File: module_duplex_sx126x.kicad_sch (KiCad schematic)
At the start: 38 parts, among them J1 USB_B_Mini, J2 Conn_01x06_Pin, J3 Conn_01x05, J4 Conn_01x04, J5 Conn_01x02_Pin, J6 Conn_01x02, SW1 SW_Push, U1 STM32F103C8Tx, U2 AMS1117-3.3, U3 SN65HVD230, U4 Ai-Thinker-Ra-02, U5 Ai-Thinker-Ra-02, Y1 16M, Y2 32.768k

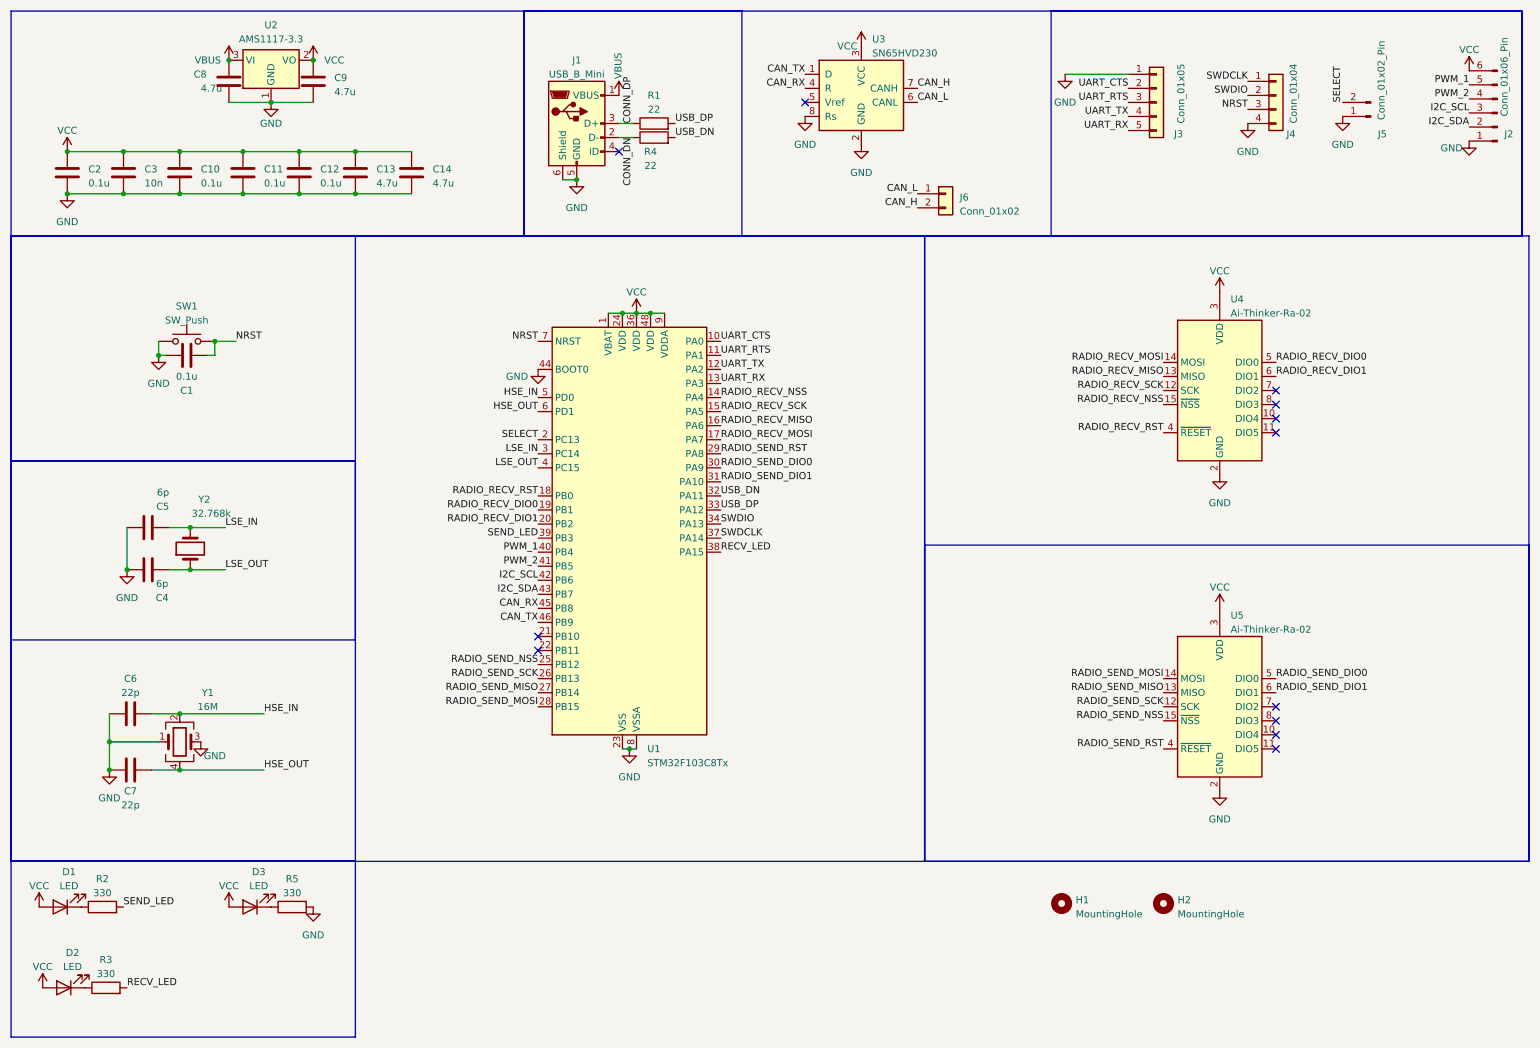
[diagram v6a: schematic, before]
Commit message: Changed connector to jumper; Added USB DM pullup
Signed-off-by: Leonardo Celente <leocelente@gmail.com>
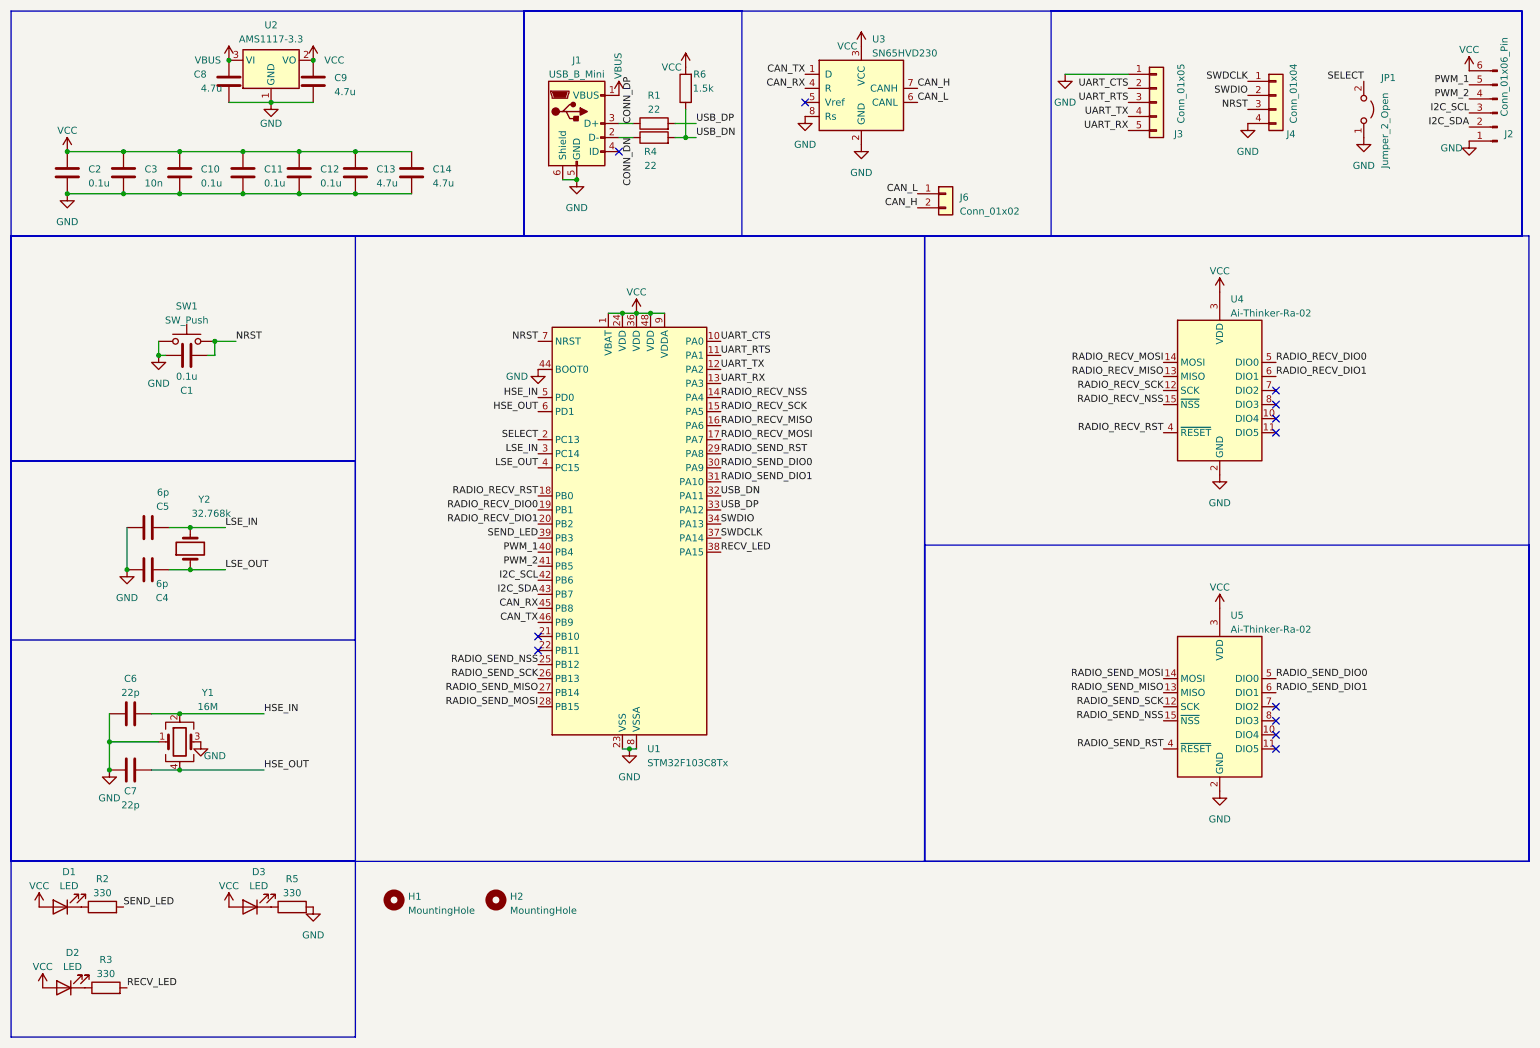
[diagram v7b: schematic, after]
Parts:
- removed J5: Conn_01x02_Pin, Connector_PinHeader_2.54mm:PinHeader_1x02_P2.54mm_Vertical, symbol Connector:Conn_01x02_Pin
- added JP1: Jumper_2_Open, Connector_PinHeader_2.54mm:PinHeader_1x02_P2.54mm_Vertical, symbol Jumper:Jumper_2_Open
- added R6: 1.5k, Resistor_SMD:R_0603_1608Metric, symbol Device:R
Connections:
- net GND: now also JP1.1 (A)
- net SELECT: now also JP1.2 (B)
- net USB_DN: now also R6.1
- net VCC: now also R6.2
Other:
- company: (none) -> Zenith Aerospace (@zenitheesc)
- title: (none) -> SX1262 Duplex USB Module
- moved on the sheet: H1, H2
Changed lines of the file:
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@@
 (kicad_sch (version 20230121) (generator eeschema)
   (paper "A4")
+  (title_block
+    (title "SX1262 Duplex USB Module")
+    (date "2023-05-20")
+    (rev "A")
+    (company "Zenith Aerospace (@zenitheesc)")
+    (comment 1 "Leonardo Celente (@leocelente)")
+  )
   (junction (at 73.66 38.1) (diameter 0) (color 0 0 0 0)
   )
@@
   (junction (at 113.665 43.18) (diameter 0) (color 0 0 0 0)
   )
+  (junction (at 133.35 35.56) (diameter 0) (color 0 0 0 0)
+  )
   (junction (at 121.92 67.31) (diameter 0) (color 0 0 0 0)
   )
@@
     (stroke (width 0) (type default))
   )
+  (wire (pts (xy 133.35 35.56) (xy 131.445 35.56))
+    (stroke (width 0) (type default))
+  )
+  (wire (pts (xy 133.35 30.48) (xy 133.35 35.56))
+    (stroke (width 0) (type default))
+  )
   (wire (pts (xy 73.66 38.1) (xy 83.82 38.1))
     (stroke (width 0) (type default))
@@
     (stroke (width 0) (type default))
   )
+  (wire (pts (xy 135.255 33.02) (xy 131.445 33.02))
+    (stroke (width 0) (type default))
+  )
   (wire (pts (xy 36.83 139.7) (xy 41.91 139.7))
     (stroke (width 0) (type default))
@@
     (stroke (width 0) (type default))
   )
+  (wire (pts (xy 135.255 35.56) (xy 133.35 35.56))
+    (stroke (width 0) (type default))
+  )
   (wire (pts (xy 41.91 45.72) (xy 53.34 45.72))
     (stroke (width 0) (type default))
@@
     (effects (font (size 1.27 1.27)) (justify right bottom))
   )
-  (label "USB_DN" (at 131.445 35.56 0) (fields_autoplaced)
+  (label "USB_DN" (at 135.255 35.56 0) (fields_autoplaced)
     (effects (font (size 1.27 1.27)) (justify left bottom))
   )
@@
     (effects (font (size 1.27 1.27)) (justify left bottom))
   )
-  (label "SELECT" (at 252.095 29.21 90) (fields_autoplaced)
-    (effects (font (size 1.27 1.27)) (justify left bottom))
+  (label "SELECT" (at 255.905 25.4 180) (fields_autoplaced)
+    (effects (font (size 1.27 1.27)) (justify right bottom))
   )
   (label "RADIO_RECV_MOSI" (at 139.7 90.17 0) (fields_autoplaced)
@@
     (effects (font (size 1.27 1.27)) (justify left bottom))
   )
-  (label "USB_DP" (at 131.445 33.02 0) (fields_autoplaced)
+  (label "USB_DP" (at 135.255 33.02 0) (fields_autoplaced)
     (effects (font (size 1.27 1.27)) (justify left bottom))
   )
@@
     )
   )
+  (symbol (lib_id "power:VCC") (at 133.35 22.86 0) (unit 1)
+    (in_bom yes) (on_board yes) (dnp no)
+    (property "Reference" "#PWR031" (at 133.35 26.67 0)
+      (effects (font (size 1.27 1.27)) hide)
+    )
+    (property "Value" "VCC" (at 130.81 22.86 0)
+      (effects (font (size 1.27 1.27)))
+    )
+    (property "Footprint" "" (at 133.35 22.86 0)
+      (effects (font (size 1.27 1.27)) hide)
+    )
+    (property "Datasheet" "" (at 133.35 22.86 0)
+      (effects (font (size 1.27 1.27)) hide)
+    )
+    (pin "1")
+    (instances
+      (project "module_duplex_sx126x"
+        (path "/cad4c6e2-312a-4b4d-83a4-aea5cc498c0d"
+          (reference "#PWR031") (unit 1)
+        )
+      )
+    )
+  )
   (symbol (lib_id "power:VCC") (at 66.04 21.59 0) (unit 1)
     (in_bom yes) (on_board yes) (dnp no)
@@
     )
   )
-  (symbol (lib_id "power:GND") (at 252.095 31.75 0) (unit 1)
+  (symbol (lib_id "power:GND") (at 255.905 35.56 0) (unit 1)
     (in_bom yes) (on_board yes) (dnp no)
-    (property "Reference" "#PWR024" (at 252.095 38.1 0)
+    (property "Reference" "#PWR024" (at 255.905 41.91 0)
       (effects (font (size 1.27 1.27)) hide)
     )
-    (property "Value" "GND" (at 252.095 36.83 0)
+    (property "Value" "GND" (at 255.905 40.64 0)
       (effects (font (size 1.27 1.27)))
     )
-    (property "Footprint" "" (at 252.095 31.75 0)
+    (property "Footprint" "" (at 255.905 35.56 0)
       (effects (font (size 1.27 1.27)) hide)
     )
-    (property "Datasheet" "" (at 252.095 31.75 0)
+    (property "Datasheet" "" (at 255.905 35.56 0)
       (effects (font (size 1.27 1.27)) hide)
     )
@@
     )
   )
+  (symbol (lib_id "Device:R") (at 133.35 26.67 180) (unit 1)
+    (in_bom yes) (on_board yes) (dnp no)
+    (property "Reference" "R6" (at 135.89 24.13 0)
+      (effects (font (size 1.27 1.27)))
+    )
+    (property "Value" "1.5k" (at 136.525 26.67 0)
+      (effects (font (size 1.27 1.27)))
+    )
+    (property "Footprint" "Resistor_SMD:R_0603_1608Metric" (at 135.128 26.67 90)
+      (effects (font (size 1.27 1.27)) hide)
+    )
+    (property "Datasheet" "~" (at 133.35 26.67 0)
+      (effects (font (size 1.27 1.27)) hide)
+    )
+    (property "LCSC" "C22843" (at 133.35 26.67 90)
+      (effects (font (size 1.27 1.27)) hide)
+    )
+    (property "Aoba" "" (at 133.35 26.67 0)
+      (effects (font (size 1.27 1.27)) hide)
+    )
+    (pin "1")
+    (pin "2")
+    (instances
+      (project "module_duplex_sx126x"
+        (path "/cad4c6e2-312a-4b4d-83a4-aea5cc498c0d"
+          (reference "R6") (unit 1)
+        )
+      )
+    )
+  )
   (symbol (lib_id "power:GND") (at 45.72 144.78 0) (unit 1)
     (in_bom yes) (on_board yes) (dnp no)
@@
     )
   )
-  (symbol (lib_id "Mechanical:MountingHole") (at 219.71 173.99 0) (unit 1)
+  (symbol (lib_id "Mechanical:MountingHole") (at 99.06 173.355 0) (unit 1)
     (in_bom no) (on_board yes) (dnp no) (fields_autoplaced)
-    (property "Reference" "H2" (at 222.25 173.355 0)
+    (property "Reference" "H2" (at 101.6 172.72 0)
       (effects (font (size 1.27 1.27)) (justify left))
     )
-    (property "Value" "MountingHole" (at 222.25 175.895 0)
+    (property "Value" "MountingHole" (at 101.6 175.26 0)
       (effects (font (size 1.27 1.27)) (justify left))
     )
-    (property "Footprint" "MountingHole:MountingHole_3.2mm_M3_Pad" (at 219.71 173.99 0)
+    (property "Footprint" "MountingHole:MountingHole_3.2mm_M3_Pad" (at 99.06 173.355 0)
       (effects (font (size 1.27 1.27)) hide)
     )
-    (property "Datasheet" "~" (at 219.71 173.99 0)
+    (property "Datasheet" "~" (at 99.06 173.355 0)
       (effects (font (size 1.27 1.27)) hide)
     )
@@
     )
   )
-  (symbol (lib_id "Connector:Conn_01x02_Pin") (at 257.175 31.75 180) (unit 1)
-    (in_bom no) (on_board yes) (dnp no)
-    (property "Reference" "J5" (at 258.445 34.925 0)
-      (effects (font (size 1.27 1.27)) (justify right))
-    )
-    (property "Value" "Conn_01x02_Pin" (at 259.08 32.385 90)
-      (effects (font (size 1.27 1.27)) (justify right))
-    )
-    (property "Footprint" "Connector_PinHeader_2.54mm:PinHeader_1x02_P2.54mm_Vertical" (at 257.175 31.75 0)
-      (effects (font (size 1.27 1.27)) hide)
-    )
-    (property "Datasheet" "~" (at 257.175 31.75 0)
-      (effects (font (size 1.27 1.27)) hide)
-    )
-    (pin "1")
-    (pin "2")
-    (instances
-      (project "module_duplex_sx126x"
-        (path "/cad4c6e2-312a-4b4d-83a4-aea5cc498c0d"
-          (reference "J5") (unit 1)
-        )
-      )
-    )
-  )
   (symbol (lib_id "power:GND") (at 234.95 33.02 0) (unit 1)
     (in_bom yes) (on_board yes) (dnp no)
@@
     )
   )
+  (symbol (lib_id "Jumper:Jumper_2_Open") (at 255.905 30.48 270) (mirror x) (unit 1)
+    (in_bom no) (on_board yes) (dnp no)
+    (property "Reference" "JP1" (at 260.35 24.765 90)
+      (effects (font (size 1.27 1.27)))
+    )
+    (property "Value" "Jumper_2_Open" (at 259.715 34.29 0)
+      (effects (font (size 1.27 1.27)))
+    )
+    (property "Footprint" "Connector_PinHeader_2.54mm:PinHeader_1x02_P2.54mm_Vertical" (at 255.905 30.48 0)
+      (effects (font (size 1.27 1.27)) hide)
+    )
+    (property "Datasheet" "~" (at 255.905 30.48 0)
+      (effects (font (size 1.27 1.27)) hide)
+    )
+    (property "Aoba" "" (at 255.905 30.48 0)
+      (effects (font (size 1.27 1.27)) hide)
+    )
+    (pin "1")
+    (pin "2")
+    (instances
+      (project "module_duplex_sx126x"
+        (path "/cad4c6e2-312a-4b4d-83a4-aea5cc498c0d"
+          (reference "JP1") (unit 1)
+        )
+      )
+    )
+  )
   (symbol (lib_id "Regulator_Linear:AMS1117-3.3") (at 58.42 21.59 0) (unit 1)
     (in_bom yes) (on_board yes) (dnp no) (fields_autoplaced)
@@
     )
   )
-  (symbol (lib_id "Mechanical:MountingHole") (at 201.295 173.99 0) (unit 1)
+  (symbol (lib_id "Mechanical:MountingHole") (at 80.645 173.355 0) (unit 1)
     (in_bom no) (on_board yes) (dnp no) (fields_autoplaced)
-    (property "Reference" "H1" (at 203.835 173.355 0)
+    (property "Reference" "H1" (at 83.185 172.72 0)
       (effects (font (size 1.27 1.27)) (justify left))
     )
-    (property "Value" "MountingHole" (at 203.835 175.895 0)
+    (property "Value" "MountingHole" (at 83.185 175.26 0)
       (effects (font (size 1.27 1.27)) (justify left))
     )
-    (property "Footprint" "MountingHole:MountingHole_3.2mm_M3_Pad" (at 201.295 173.99 0)
+    (property "Footprint" "MountingHole:MountingHole_3.2mm_M3_Pad" (at 80.645 173.355 0)
       (effects (font (size 1.27 1.27)) hide)
     )
-    (property "Datasheet" "~" (at 201.295 173.99 0)
+    (property "Datasheet" "~" (at 80.645 173.355 0)
       (effects (font (size 1.27 1.27)) hide)
     )

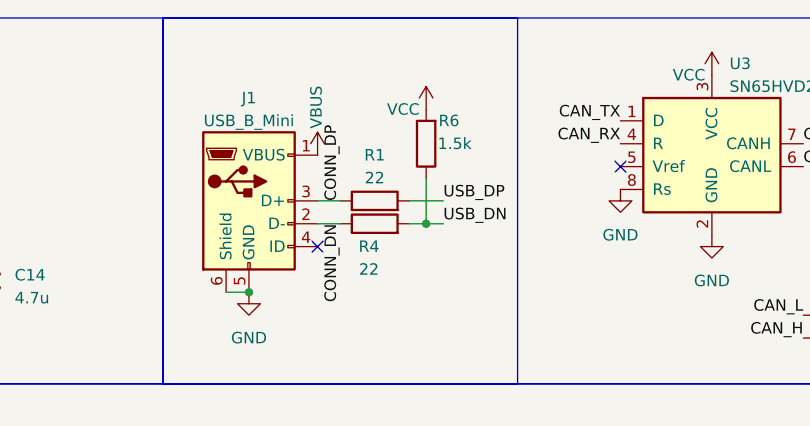
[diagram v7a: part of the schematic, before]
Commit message: Moved pull up to correct USB_DP
Signed-off-by: Leonardo Celente <leocelente@gmail.com>
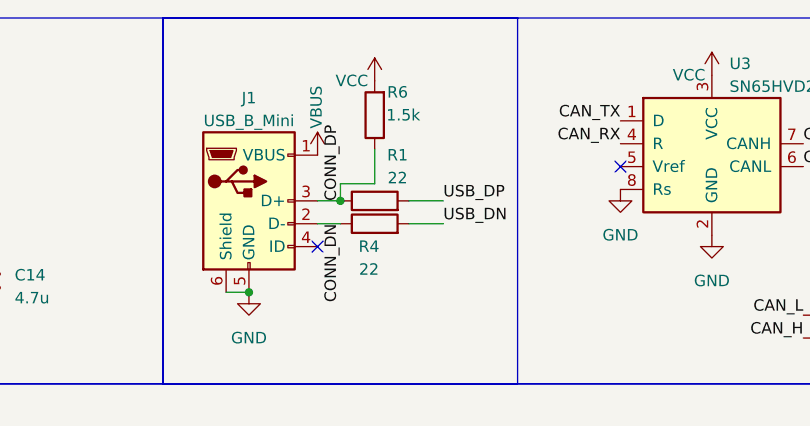
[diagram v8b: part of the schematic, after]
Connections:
- net CONN_DP: now also R6.1
- net USB_DN: no longer R6.1
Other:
- moved on the sheet: R6
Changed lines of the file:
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@@
   (junction (at 113.665 43.18) (diameter 0) (color 0 0 0 0)
   )
-  (junction (at 133.35 35.56) (diameter 0) (color 0 0 0 0)
-  )
   (junction (at 121.92 67.31) (diameter 0) (color 0 0 0 0)
+  )
+  (junction (at 123.825 33.02) (diameter 0) (color 0 0 0 0)
   )
   (junction (at 48.26 72.39) (diameter 0) (color 0 0 0 0)
@@
     (stroke (width 0) (type default))
   )
+  (wire (pts (xy 131.445 33.02) (xy 135.255 33.02))
+    (stroke (width 0) (type default))
+  )
   (wire (pts (xy 53.34 45.72) (xy 63.5 45.72))
     (stroke (width 0) (type default))
@@
     (stroke (width 0) (type default))
   )
+  (wire (pts (xy 127.635 31.115) (xy 123.825 31.115))
+    (stroke (width 0) (type default))
+  )
+  (wire (pts (xy 123.825 31.115) (xy 123.825 33.02))
+    (stroke (width 0) (type default))
+  )
   (wire (pts (xy 63.5 38.1) (xy 73.66 38.1))
     (stroke (width 0) (type default))
@@
     (stroke (width 0) (type default))
   )
-  (wire (pts (xy 133.35 35.56) (xy 131.445 35.56))
-    (stroke (width 0) (type default))
-  )
-  (wire (pts (xy 133.35 30.48) (xy 133.35 35.56))
+  (wire (pts (xy 131.445 35.56) (xy 135.255 35.56))
     (stroke (width 0) (type default))
   )
@@
     (stroke (width 0) (type default))
   )
-  (wire (pts (xy 135.255 33.02) (xy 131.445 33.02))
-    (stroke (width 0) (type default))
-  )
   (wire (pts (xy 36.83 139.7) (xy 41.91 139.7))
     (stroke (width 0) (type default))
@@
     (stroke (width 0) (type default))
   )
-  (wire (pts (xy 135.255 35.56) (xy 133.35 35.56))
-    (stroke (width 0) (type default))
-  )
   (wire (pts (xy 41.91 45.72) (xy 53.34 45.72))
     (stroke (width 0) (type default))
@@
   )
   (wire (pts (xy 124.46 67.31) (xy 127 67.31))
+    (stroke (width 0) (type default))
+  )
+  (wire (pts (xy 127.635 27.305) (xy 127.635 31.115))
     (stroke (width 0) (type default))
   )
@@
     )
   )
-  (symbol (lib_id "power:VCC") (at 133.35 22.86 0) (unit 1)
+  (symbol (lib_id "power:VCC") (at 127.635 19.685 0) (unit 1)
     (in_bom yes) (on_board yes) (dnp no)
-    (property "Reference" "#PWR031" (at 133.35 26.67 0)
-      (effects (font (size 1.27 1.27)) hide)
-    )
-    (property "Value" "VCC" (at 130.81 22.86 0)
-      (effects (font (size 1.27 1.27)))
-    )
-    (property "Footprint" "" (at 133.35 22.86 0)
-      (effects (font (size 1.27 1.27)) hide)
-    )
-    (property "Datasheet" "" (at 133.35 22.86 0)
+    (property "Reference" "#PWR031" (at 127.635 23.495 0)
+      (effects (font (size 1.27 1.27)) hide)
+    )
+    (property "Value" "VCC" (at 125.095 19.685 0)
+      (effects (font (size 1.27 1.27)))
+    )
+    (property "Footprint" "" (at 127.635 19.685 0)
+      (effects (font (size 1.27 1.27)) hide)
+    )
+    (property "Datasheet" "" (at 127.635 19.685 0)
       (effects (font (size 1.27 1.27)) hide)
     )
@@
   )
   (symbol (lib_id "Device:R") (at 127.635 33.02 90) (unit 1)
-    (in_bom yes) (on_board yes) (dnp no) (fields_autoplaced)
-    (property "Reference" "R1" (at 127.635 27.94 90)
-      (effects (font (size 1.27 1.27)))
-    )
-    (property "Value" "22" (at 127.635 30.48 90)
+    (in_bom yes) (on_board yes) (dnp no)
+    (property "Reference" "R1" (at 130.175 27.94 90)
+      (effects (font (size 1.27 1.27)))
+    )
+    (property "Value" "22" (at 130.175 30.48 90)
       (effects (font (size 1.27 1.27)))
     )
@@
     )
   )
-  (symbol (lib_id "Device:R") (at 133.35 26.67 180) (unit 1)
+  (symbol (lib_id "Device:R") (at 127.635 23.495 180) (unit 1)
     (in_bom yes) (on_board yes) (dnp no)
-    (property "Reference" "R6" (at 135.89 24.13 0)
-      (effects (font (size 1.27 1.27)))
-    )
-    (property "Value" "1.5k" (at 136.525 26.67 0)
-      (effects (font (size 1.27 1.27)))
-    )
-    (property "Footprint" "Resistor_SMD:R_0603_1608Metric" (at 135.128 26.67 90)
-      (effects (font (size 1.27 1.27)) hide)
-    )
-    (property "Datasheet" "~" (at 133.35 26.67 0)
-      (effects (font (size 1.27 1.27)) hide)
-    )
-    (property "LCSC" "C22843" (at 133.35 26.67 90)
-      (effects (font (size 1.27 1.27)) hide)
-    )
-    (property "Aoba" "" (at 133.35 26.67 0)
-      (effects (font (size 1.27 1.27)) hide)
-    )
+    (property "Reference" "R6" (at 130.175 20.955 0)
+      (effects (font (size 1.27 1.27)))
+    )
+    (property "Value" "1.5k" (at 130.81 23.495 0)
+      (effects (font (size 1.27 1.27)))
+    )
+    (property "Footprint" "Resistor_SMD:R_0603_1608Metric" (at 129.413 23.495 90)
+      (effects (font (size 1.27 1.27)) hide)
+    )
+    (property "Datasheet" "~" (at 127.635 23.495 0)
+      (effects (font (size 1.27 1.27)) hide)
+    )
+    (property "LCSC" "C22843" (at 127.635 23.495 90)
+      (effects (font (size 1.27 1.27)) hide)
+    )
+    (property "Aoba" "" (at 127.635 23.495 0)
+      (effects (font (size 1.27 1.27)) hide)
+    )
